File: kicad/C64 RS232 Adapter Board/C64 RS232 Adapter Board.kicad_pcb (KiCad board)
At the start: 2 copper layers, 63.6 x 56.9 mm, 31 parts, among them J1 RS232_HDR, J2 DB25_RS232, J3 C64_USER_PORT, J4 User Port Breakout, SW1 RESET, U1 MAX3241ECAI+T

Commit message: before first routing attempt
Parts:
- moved JP12 21.6 mm to (61.0, 72.6), turned to 270 degrees
- moved JP13 14.5 mm to (63.1, 72.8), turned to 270 degrees
- moved H2 13.4 mm to (88.2, 56.1)
- moved H3 13.4 mm to (88.2, 105.7)
- moved J2 13.4 mm to (91.4, 80.2)
- moved C2 13.3 mm to (68.4, 86.8), turned to 270 degrees
- moved C4 11.9 mm to (66.5, 86.8), turned to 90 degrees
- moved C3 11.9 mm to (70.4, 75.0), turned to 270 degrees
- moved C5 11.1 mm to (66.1, 71.8), turned to 0 degrees
- moved JP1 11.1 mm to (74.2, 70.7), turned to 0 degrees
- moved JP8 11.1 mm to (74.1, 73.2), turned to 180 degrees
- moved C1 9.43 mm to (67.0, 73.7), turned to 0 degrees
- moved D1 5.28 mm to (63.5, 105.0)
- moved R1 5.28 mm to (66.7, 105.0)
- moved R2 5.28 mm to (81.9, 105.0)
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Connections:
- C1 pad 1: Net-(C1-Pad1) -> (no net)
- C1 pad 2: Net-(C1-Pad2) -> (no net)
- C2 pad 1: Net-(C2-Pad1) -> (no net)
- C2 pad 2: Net-(C2-Pad2) -> (no net)
- C3 pad 1: GND -> (no net)
- C3 pad 2: Net-(C3-Pad2) -> (no net)
- C4 pad 1: GND -> (no net)
- C4 pad 2: Net-(C4-Pad2) -> (no net)
- C5 pad 1: GND -> (no net)
- C5 pad 2: +5V -> (no net)
- JP13 pad 1: Net-(JP13-Pad1) -> (no net)
- JP13 pad 2: +5V -> (no net)
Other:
- board size 63.6 x 56.9 mm -> 50.2 x 57.1 mm

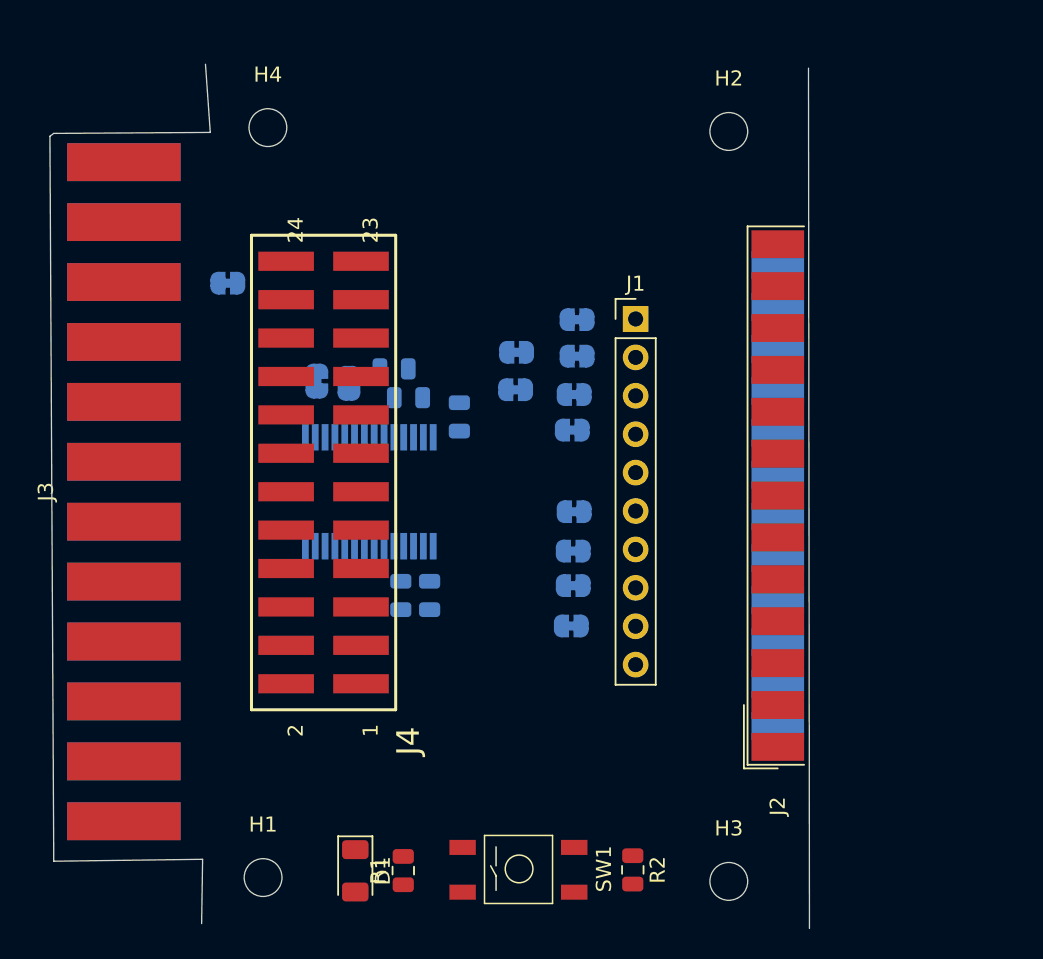
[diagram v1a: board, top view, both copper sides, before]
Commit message: Tried this layout but don't like it
Instead of going a 2nd time, going to try creating two boards instead
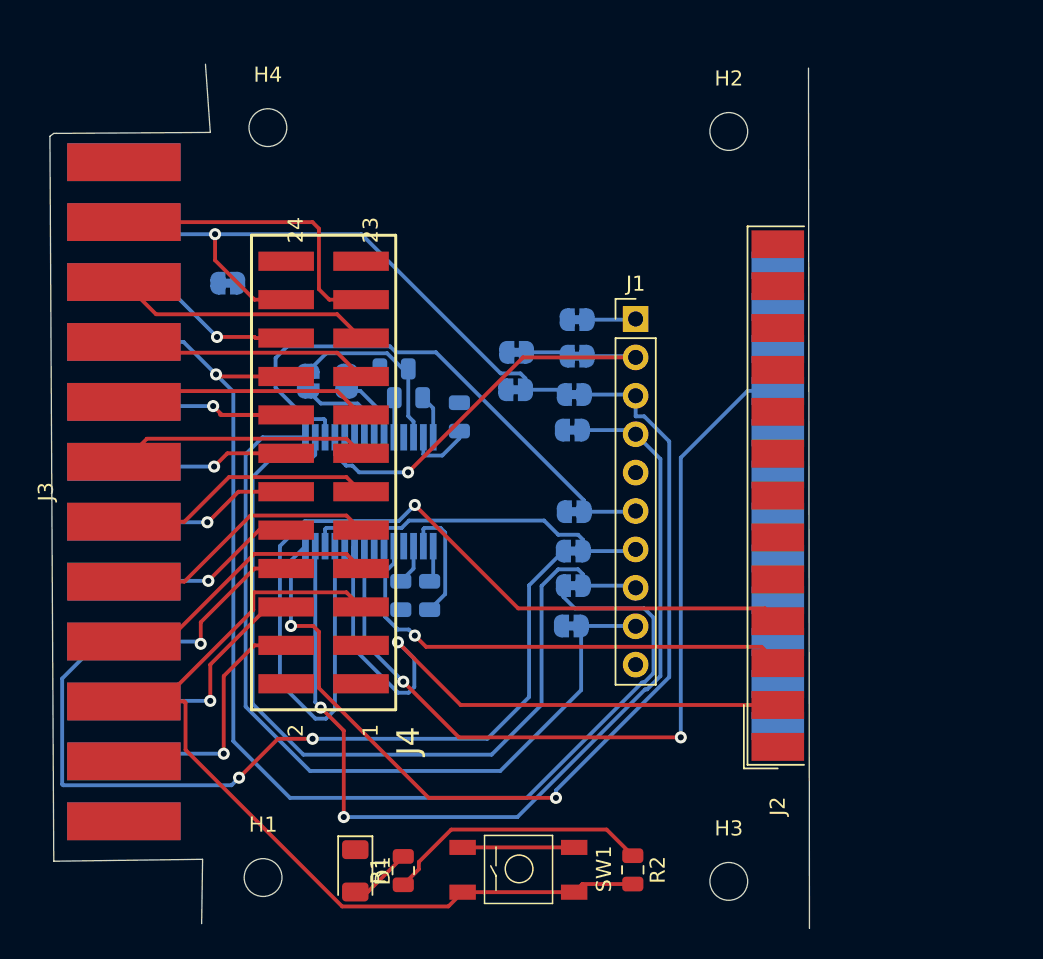
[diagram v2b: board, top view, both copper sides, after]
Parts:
- moved JP13 2.70 mm to (60.4, 72.6), turned to 90 degrees
- moved JP12 1.97 mm to (62.9, 72.6)
- turned JP10 to 0 degrees
- turned JP4 to 0 degrees
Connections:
- C1 pad 1: (no net) -> Net-(C1-Pad1)
- C1 pad 2: (no net) -> Net-(C1-Pad2)
- C2 pad 1: (no net) -> Net-(C2-Pad1)
- C2 pad 2: (no net) -> Net-(C2-Pad2)
- C3 pad 1: (no net) -> GND
- C3 pad 2: (no net) -> Net-(C3-Pad2)
- C4 pad 1: (no net) -> GND
- C4 pad 2: (no net) -> Net-(C4-Pad2)
- C5 pad 1: (no net) -> GND
- C5 pad 2: (no net) -> +5V
- JP13 pad 1: (no net) -> Net-(JP13-Pad1)
- JP13 pad 2: (no net) -> +5V
- R2 pad 2: Net-(R2-Pad2) -> /RESET
- SW1 pad 1: Net-(R2-Pad2) -> /RESET
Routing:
- net /PB6: track 0.00 -> 80.1 mm, vias 0 -> 1
- net /PB1: track 0.00 -> 69.7 mm, vias 0 -> 3
- net /TXD_TTL: track 0.00 -> 64.5 mm, vias 0 -> 2
- net /DTR_TTL: track 0.00 -> 63.8 mm, vias 0 -> 2
- net /RTS_232: track 0.00 -> 62.0 mm, vias 0 -> 1
- net /RESET: track 0.00 -> 61.4 mm
- net /CTS_TTL: track 0.00 -> 58.3 mm
- net /RI_232: track 0.00 -> 56.6 mm, vias 0 -> 2
- net /RI_TTL: track 0.00 -> 55.1 mm
- net /TXD_232: track 0.00 -> 42.4 mm, vias 0 -> 1
- net /PA2: track 0.00 -> 41.8 mm, vias 0 -> 1
- net /DSR_TTL: track 0.00 -> 36.4 mm
- net /RXD_232: track 0.00 -> 32.1 mm, vias 0 -> 1
- net +5V: track 0.00 -> 29.9 mm
- net /RXD_TTL: track 0.00 -> 27.9 mm, vias 0 -> 1
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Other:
- net class Default: clearance 0.2 -> 0.2032; trace_width 0.25 -> 0.254
- rule trace_clearance: 0.2 -> 0.2032
- board text added: "TODO: Recenter Breakout Pins to the edge connector +/- 9VAC thicker traces... about 20mil? Move MAX32's caps to top side Try routing with MAX32 rotated 180 VIAs right off the SMT header for bottom side of card See which jumpers can go to front side (ones without a 232 connection)"

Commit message: added vias
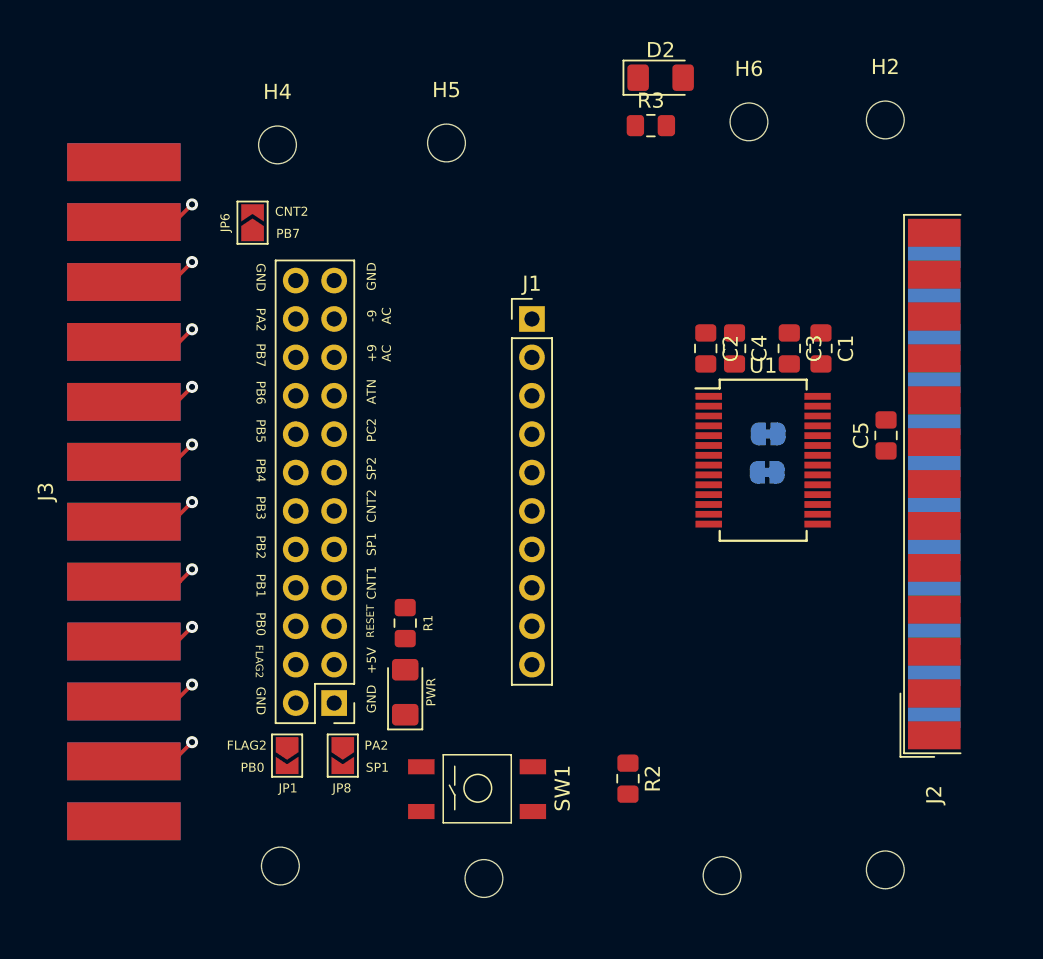
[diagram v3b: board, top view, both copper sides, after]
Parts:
- removed JP10, JP11, JP2, JP3, JP4, JP5, JP7, JP9: SolderJumper_2_Bridged, Jumper:SolderJumper-2_P1.3mm_Bridged_RoundedPad1.0x1.5mm
- added D2: 232-PWR, LED_SMD:LED_1206_3216Metric_Pad1.42x1.75mm_HandSolder, F.Cu at (83.7, 52.6)
- added H5: MountingHole, MountingHole:MountingHole_2.5mm, F.Cu at (69.5, 56.9)
- added H6: MountingHole, MountingHole:MountingHole_2.5mm, F.Cu at (89.5, 55.5)
- added H7: MountingHole, MountingHole:MountingHole_2.5mm, F.Cu at (72.0, 105.5)
- added H8: MountingHole, MountingHole:MountingHole_2.5mm, F.Cu at (87.8, 105.3)
- added R3: 1K, Resistor_SMD:R_0805_2012Metric_Pad1.15x1.40mm_HandSolder, F.Cu at (83.0, 55.7)
- C1, C2, C3, C4, C5: footprint Capacitor_SMD:C_0805_2012Metric -> Capacitor_SMD:C_0805_2012Metric_Pad1.15x1.40mm_HandSolder; moved to F.Cu
- J4: footprint My Libraries:TSM-for-C64-User-Port -> My Libraries:C64_2.54mm_User_Port
- JP1, JP6, JP8: footprint Jumper:SolderJumper-2_P1.3mm_Bridged_RoundedPad1.0x1.5mm -> Jumper:SolderJumper-2_P1.3mm_Open_TrianglePad1.0x1.5mm; moved to F.Cu
- PWR: renamed from D1; value PWR -> C64-PWR; footprint LED_SMD:LED_1206_3216Metric -> LED_SMD:LED_1206_3216Metric_Pad1.42x1.75mm_HandSolder
- R1, R2: footprint Resistor_SMD:R_0805_2012Metric -> Resistor_SMD:R_0805_2012Metric_Pad1.15x1.40mm_HandSolder
- U1: moved to F.Cu
- moved C5 32.8 mm to (98.6, 76.2), turned to 90 degrees
- moved JP13 30.9 mm to (90.7, 78.7), turned to 0 degrees
- moved JP1 30.7 mm to (59.0, 97.4), turned to 270 degrees
- moved JP12 28.1 mm to (90.8, 76.1), turned to 0 degrees
- moved C1 27.5 mm to (94.3, 70.5), turned to 270 degrees
- moved C4 27.5 mm to (88.6, 70.5), turned to 270 degrees
- moved JP8 26.8 mm to (62.7, 97.4), turned to 270 degrees
- moved U1 26.1 mm to (90.5, 77.9), turned to 0 degrees
- moved C2 24.5 mm to (86.7, 70.5)
- moved C3 22.3 mm to (92.2, 70.5)
- moved R1 16.4 mm to (66.8, 88.6), turned to 270 degrees
- moved J4 15.3 mm to (62.1, 93.9), turned to 180 degrees
- moved PWR 12.3 mm to (66.8, 93.2), turned to 90 degrees
- moved H2 10.4 mm to (98.6, 55.4)
- moved H3 10.4 mm to (98.6, 105.0)
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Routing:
- net /PB6: track 80.1 -> 0.00 mm, vias 1 -> 0
- net /PB1: track 69.7 -> 0.00 mm, vias 3 -> 0
- net /TXD_TTL: track 64.5 -> 0.00 mm, vias 2 -> 0
- net /DTR_TTL: track 63.8 -> 0.00 mm, vias 2 -> 0
- net /RTS_232: track 62.0 -> 0.00 mm, vias 1 -> 0
- net /CTS_TTL: track 58.3 -> 0.00 mm
- net /RI_232: track 56.6 -> 0.00 mm, vias 2 -> 0
- net /RESET: track 61.4 -> 4.97 mm, vias 0 -> 1
- net /RI_TTL: track 55.1 -> 0.00 mm
- net /TXD_232: track 42.4 -> 0.00 mm, vias 1 -> 0
- net /PA2: track 41.8 -> 0.00 mm, vias 1 -> 0
- net /DSR_TTL: track 36.4 -> 0.00 mm
- net /RXD_232: track 32.1 -> 0.00 mm, vias 1 -> 0
- net /RXD_TTL: track 27.9 -> 0.00 mm, vias 1 -> 0
- net +5V: track 29.9 -> 5.03 mm, vias 0 -> 1
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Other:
- board outline removed
- board text added: "+5V"
- board text added: "+9 AC"
- board text added: "-9 AC"
- board text added: "ATN"
- board text added: "CNT1"
- board text added: "CNT2"
- board text added: "FLAG2"
- board text added: "GND"
- board text added: "PA2"
- board text added: "PB0"
- board text added: "PB1"
- board text added: "PB2"
- board text added: "PB3"
- board text added: "PB4"
- board text added: "PB5"
- board text added: "PB6"
- board text added: "PB7"
- board text added: "PC2"
- board text added: "RESET"
- board text added: "SP1"
- board text added: "SP2"
- board text removed: "TODO: Recenter Breakout Pins to the edge connector +/- 9VAC thicker traces... about 20mil? Move MAX32's caps to top side Try routing with MAX32 rotated 180 VIAs right off the SMT header for bottom side of card See which jumpers can go to front side (ones without a 232 connection)"

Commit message: moved pinouts around
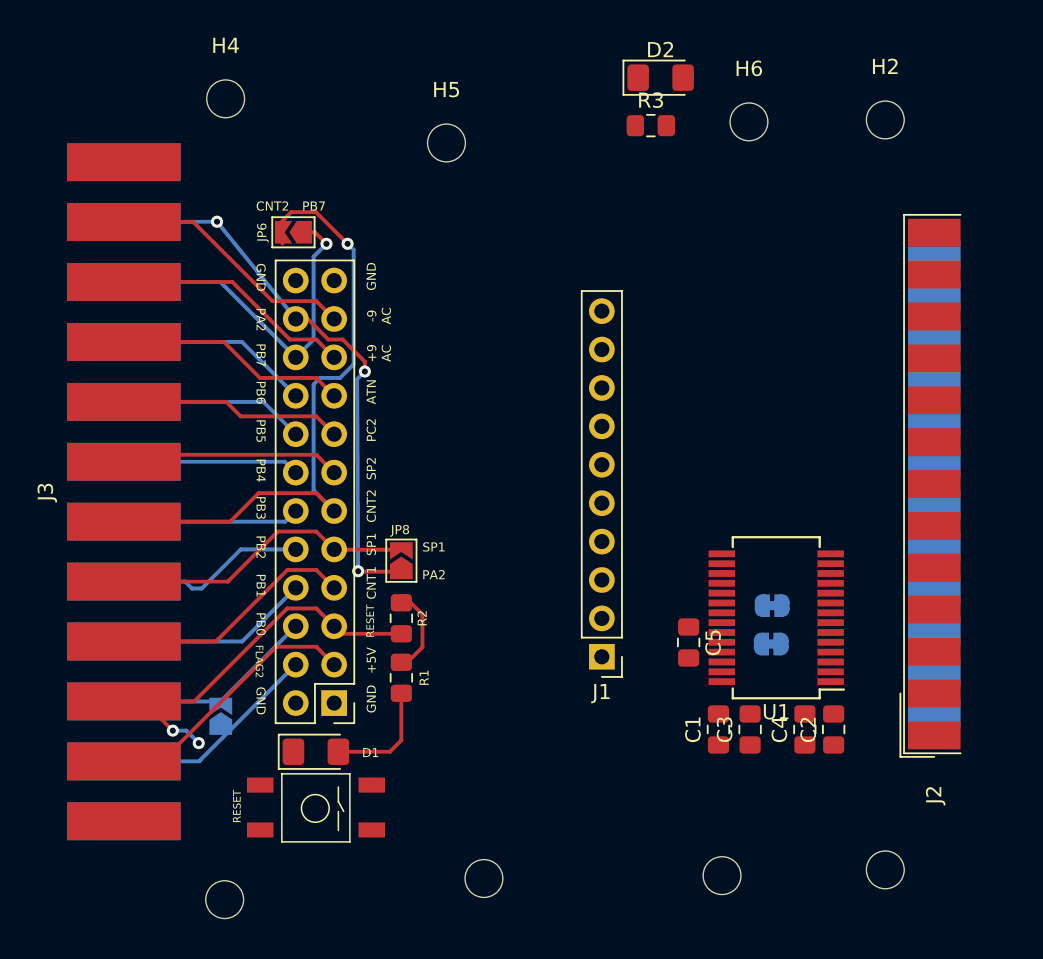
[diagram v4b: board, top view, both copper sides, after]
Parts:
- JP1: moved to B.Cu
- moved C2 26.6 mm to (95.1, 95.7), turned to 90 degrees
- moved C1 26.1 mm to (87.5, 95.7), turned to 90 degrees
- moved C4 25.6 mm to (93.2, 95.7), turned to 90 degrees
- moved C3 25.3 mm to (89.6, 95.7), turned to 90 degrees
- moved J1 22.8 mm to (79.8, 90.9), turned to 180 degrees
- moved C5 18.9 mm to (85.5, 89.9), turned to 270 degrees
- moved R2 18.4 mm to (66.5, 88.3)
- moved JP12 13.9 mm to (91.0, 90.0), turned to 180 degrees
- moved JP8 13.5 mm to (66.5, 84.5), turned to 90 degrees
- moved SW1 10.9 mm to (60.8, 100.9), turned to 270 degrees
- moved U1 10.5 mm to (91.3, 88.3), turned to 180 degrees
- moved JP13 8.82 mm to (91.1, 87.5), turned to 180 degrees
- moved D1 7.10 mm to (60.9, 97.2), turned to 0 degrees
- moved JP1 5.10 mm to (54.6, 94.8), turned to 90 degrees
- moved H4 4.59 mm to (54.9, 54.0)
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- renumbered PWR to D1
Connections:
- J1 pad 1: /DCD_TTL -> /TXD_TTL
- J1 pad 2: /RXD_TTL -> /DTR_TTL
- J1 pad 3: /TXD_TTL -> /RTS_TTL
- J1 pad 4: /DTR_TTL -> /RI_TTL
- J1 pad 6: /DSR_TTL -> /DCD_TTL
- J1 pad 7: /RTS_TTL -> /DSR_TTL
- J1 pad 9: /RI_TTL -> /RXD_TTL
- J2 pad 20: Net-(J2-Pad20) -> /DTR_232
- U1 pad 10: /DTR_232 -> /RTS_232
- U1 pad 11: /RTS_232 -> /DTR_232
- U1 pad 15: /RI_TTL -> /RXD_TTL
- U1 pad 18: /RXD_TTL -> /DCD_TTL
- U1 pad 19: /DCD_TTL -> /RI_TTL
- U1 pad 4: /DCD_232 -> /RI_232
- U1 pad 5: /RXD_232 -> /DCD_232
- U1 pad 8: /RI_232 -> /RXD_232
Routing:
- net /CNT2: track 5.05 -> 45.6 mm
- net /PA2: track 0.00 -> 37.1 mm, vias 0 -> 3
- net /RESET: track 4.97 -> 31.1 mm, vias 1 -> 2
- net +5V: track 5.03 -> 29.2 mm, vias 1 -> 0
- net /PB7: track 0.00 -> 23.6 mm, vias 0 -> 1
- net /SP1: track 4.85 -> 23.9 mm, vias 1 -> 0
- net /CNT1: track 4.91 -> 19.9 mm, vias 1 -> 0
- net /-9VAC: track 4.99 -> 19.9 mm, vias 1 -> 0
- net /ATN: track 4.86 -> 19.1 mm, vias 1 -> 0
- net /+9VAC: track 5.06 -> 19.2 mm, vias 1 -> 0
- net /FLAG2: track 0.00 -> 14.0 mm
- net /PB0: track 0.00 -> 13.4 mm
- net /PC2: track 4.92 -> 18.3 mm, vias 1 -> 0
- net /SP2: track 4.98 -> 18.0 mm, vias 1 -> 0
- net /PB6: track 0.00 -> 12.8 mm
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
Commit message: 232 signals routed clean
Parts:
- moved J1 22.9 mm to (80.5, 68.0), turned to 0 degrees
- moved JP12 1.45 mm to (90.2, 91.2), turned to 90 degrees
- moved JP13 1.13 mm to (90.1, 86.8), turned to 90 degrees
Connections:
- U1 pad 15: /RXD_TTL -> /RI_TTL
- U1 pad 16: /CTS_TTL -> /DCD_TTL
- U1 pad 18: /DCD_TTL -> /CTS_TTL
- U1 pad 19: /RI_TTL -> /RXD_TTL
- U1 pad 4: /RI_232 -> /RXD_232
- U1 pad 5: /DCD_232 -> /CTS_232
- U1 pad 7: /CTS_232 -> /DCD_232
- U1 pad 8: /RXD_232 -> /RI_232
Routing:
- net /RI_232: track 0.00 -> 22.3 mm, vias 0 -> 1
- net /DCD_232: track 0.18 -> 17.0 mm
- net /DTR_232: track 0.00 -> 14.4 mm, vias 0 -> 1
- net /TXD_232: track 0.19 -> 12.5 mm, vias 0 -> 2
- net /DSR_232: track 0.00 -> 11.9 mm
- net /RTS_232: track 0.00 -> 10.3 mm, vias 0 -> 2
- net /CTS_232: track 0.57 -> 10.3 mm
- net /RXD_232: track 0.00 -> 6.87 mm
- net /DTR_TTL: track 0.58 -> 0.00 mm

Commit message: First layout done
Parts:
- moved D2 51.3 mm to (89.0, 103.6)
- moved R3 45.9 mm to (89.0, 101.3)
- moved H6 11.1 mm to (78.5, 56.9)
- moved H8 9.53 mm to (78.5, 103.1)
- moved D1 5.66 mm to (66.5, 96.9), turned to 90 degrees
- moved H7 5.56 mm to (67.0, 103.1)
- moved H1 3.86 mm to (55.5, 103.1)
- moved H4 2.98 mm to (55.5, 56.9)
- moved H5 2.53 mm to (67.0, 56.9), turned to 45 degrees
- moved H3 1.84 mm to (98.6, 103.1)
- moved H2 1.52 mm to (98.6, 56.9)
- moved SW1 0.63 mm to (61.1, 101.5), turned to 180 degrees
- moved C1 0.51 mm to (87.5, 96.2)
- moved C2 0.51 mm to (95.1, 96.2)
- moved C3 0.51 mm to (89.6, 96.2)
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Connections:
- J1 pad 10: (no net) -> +5V
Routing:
- net +5V: track 29.2 -> 63.1 mm, vias 0 -> 2
- net /TXD_TTL: track 0.00 -> 25.4 mm
- net /DTR_TTL: track 0.00 -> 24.8 mm
- net /RTS_TTL: track 0.00 -> 24.0 mm
- net /RESET: track 31.1 -> 50.3 mm, vias 2 -> 3
- net /RI_TTL: track 0.00 -> 13.4 mm
- net Net-(C1-Pad1): track 0.00 -> 12.8 mm
- net Net-(C3-Pad2): track 0.00 -> 10.1 mm
- net /DCD_TTL: track 0.00 -> 10.1 mm
- net /DSR_TTL: track 0.13 -> 8.22 mm
- net /RXD_TTL: track 0.00 -> 7.92 mm
- net /CTS_TTL: track 0.00 -> 7.31 mm
- net Net-(C2-Pad1): track 0.00 -> 5.56 mm
- net Net-(D1-Pad2): track 7.58 -> 2.16 mm
- net GND: track 0.00 -> 5.25 mm, vias 0 -> 16
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- added copper zone on B.Cu, net GND
- added copper zone on F.Cu, net GND
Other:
- board outline added: 59.6 x 53.1 mm
- board text added: "PWR"
